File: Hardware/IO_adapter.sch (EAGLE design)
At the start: 20 parts, among them Y1 32Khz

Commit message: rough layout top board
I have not double checked the board to board interconect yet.
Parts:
- added PRG, RST: 6X3.5_TACT, tactile_switch:6X3.5_TACT
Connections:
- net ADCCS1: now also PRG.1
- net GND: now also PRG.2, RST.2
- net RST: now also RST.1
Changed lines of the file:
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@@
 <part name="LED1" library="adafruit" deviceset="LED" device="CHIPLED_0805"/>
 <part name="LED2" library="adafruit" deviceset="LED" device="CHIPLED_0805"/>
+<part name="PRG" library="tactile_switch" deviceset="6X3.5_TACT" device=""/>
+<part name="RST" library="tactile_switch" deviceset="6X3.5_TACT" device=""/>
+<part name="GND1" library="supply1" deviceset="GND" device=""/>
 </parts>
 <sheets>
@@
 <instance part="LED1" gate="G$1" x="86.36" y="91.44" rot="R90"/>
 <instance part="LED2" gate="G$1" x="88.9" y="86.36" rot="R270"/>
+<instance part="PRG" gate="G$1" x="223.52" y="-53.34"/>
+<instance part="RST" gate="G$1" x="223.52" y="-66.04"/>
+<instance part="GND1" gate="1" x="243.84" y="-78.74"/>
 </instances>
 <busses>
@@
 <pinref part="C7" gate="G$1" pin="2"/>
 <wire x1="261.62" y1="63.5" x2="259.08" y2="63.5" width="0.1524" layer="91"/>
+</segment>
+<segment>
+<pinref part="PRG" gate="G$1" pin="2"/>
+<wire x1="231.14" y1="-53.34" x2="243.84" y2="-53.34" width="0.1524" layer="91"/>
+<wire x1="243.84" y1="-53.34" x2="243.84" y2="-66.04" width="0.1524" layer="91"/>
+<pinref part="RST" gate="G$1" pin="2"/>
+<wire x1="243.84" y1="-66.04" x2="243.84" y2="-76.2" width="0.1524" layer="91"/>
+<wire x1="231.14" y1="-66.04" x2="243.84" y2="-66.04" width="0.1524" layer="91"/>
+<junction x="243.84" y="-66.04"/>
+<pinref part="GND1" gate="1" pin="GND"/>
 </segment>
 </net>
@@
 <label x="261.62" y="5.08" size="1.778" layer="91" font="vector" xref="yes"/>
 </segment>
+<segment>
+<pinref part="PRG" gate="G$1" pin="1"/>
+<wire x1="218.44" y1="-53.34" x2="210.82" y2="-53.34" width="0.1524" layer="91"/>
+<label x="210.82" y="-53.34" size="1.778" layer="95" rot="R180" xref="yes"/>
+</segment>
 </net>
 <net name="CSSD" class="0">
@@
 <label x="261.62" y="-17.78" size="1.778" layer="91" font="vector" xref="yes"/>
 </segment>
-</net>
+<segment>
+<pinref part="RST" gate="G$1" pin="1"/>
+<wire x1="218.44" y1="-66.04" x2="210.82" y2="-66.04" width="0.1524" layer="91"/>
+<label x="210.82" y="-66.04" size="1.778" layer="95" rot="R180" xref="yes"/>
+</segment>
+</net>

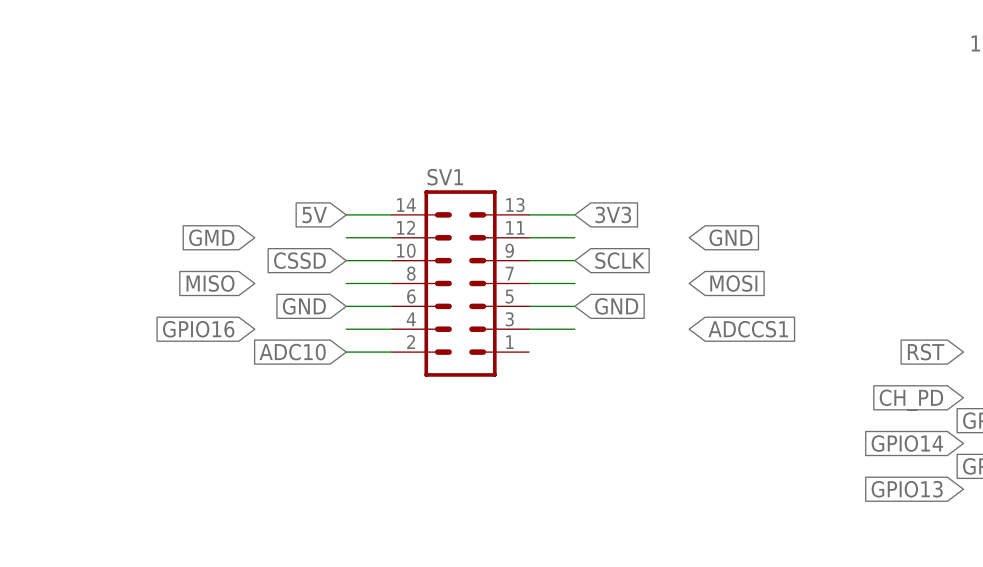
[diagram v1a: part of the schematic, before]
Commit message: completed routing for both boards
routed out both the base and IO board. Should be ready for verification
There will be errors.
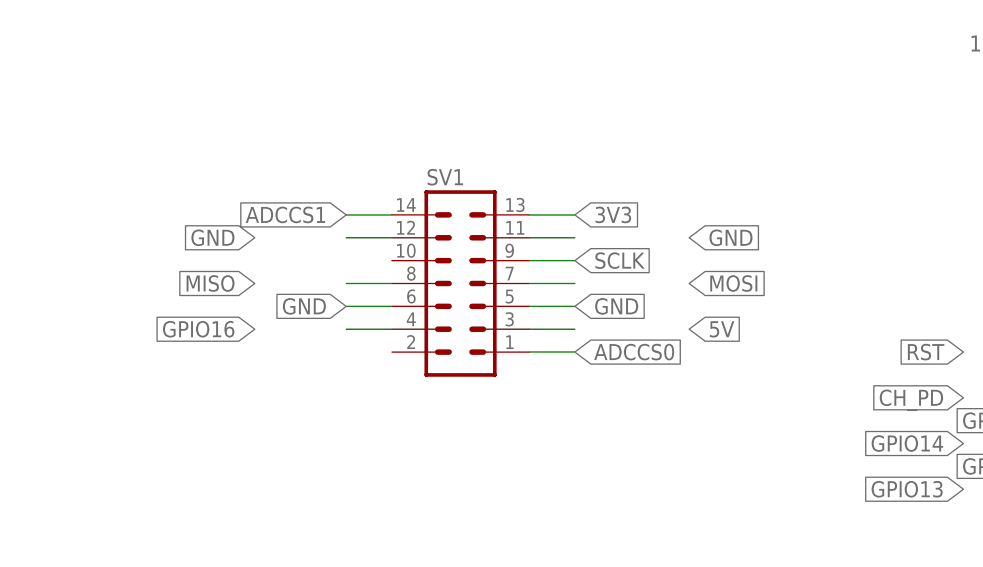
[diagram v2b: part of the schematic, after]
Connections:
- removed net ADC10: SV1.2
- removed net GMD: SV1.12
- net 5V: now also SV1.3; no longer SV1.14
- net ADCCS0: now also SV1.1
- net ADCCS1: now also SV1.14; no longer SV1.3
- net CSSD: no longer SV1.10
- net GND: now also SV1.12
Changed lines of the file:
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@@
 <pinref part="GND1" gate="1" pin="GND"/>
+</segment>
+<segment>
+<pinref part="SV1" gate="G$1" pin="12"/>
+<wire x1="71.12" y1="17.78" x2="66.04" y2="17.78" width="0.1524" layer="91"/>
+<label x="55.88" y="17.78" size="1.778" layer="91" font="vector" rot="R180" xref="yes"/>
 </segment>
 </net>
@@
 </segment>
 <segment>
-<pinref part="SV1" gate="G$1" pin="3"/>
-<wire x1="86.36" y1="7.62" x2="91.44" y2="7.62" width="0.1524" layer="91"/>
-<label x="104.14" y="7.62" size="1.778" layer="91" font="vector" xref="yes"/>
-</segment>
-<segment>
 <pinref part="U1" gate="G$1" pin="GPIO0"/>
 <wire x1="182.88" y1="-5.08" x2="187.96" y2="-5.08" width="0.1524" layer="91"/>
@@
 <wire x1="218.44" y1="-53.34" x2="210.82" y2="-53.34" width="0.1524" layer="91"/>
 <label x="210.82" y="-53.34" size="1.778" layer="95" rot="R180" xref="yes"/>
+</segment>
+<segment>
+<pinref part="SV1" gate="G$1" pin="14"/>
+<wire x1="71.12" y1="20.32" x2="66.04" y2="20.32" width="0.1524" layer="91"/>
+<label x="66.04" y="20.32" size="1.778" layer="91" rot="R180" xref="yes"/>
 </segment>
 </net>
@@
 </segment>
 <segment>
-<pinref part="SV1" gate="G$1" pin="10"/>
-<wire x1="71.12" y1="15.24" x2="66.04" y2="15.24" width="0.1524" layer="91"/>
-<label x="66.04" y="15.24" size="1.778" layer="91" font="vector" rot="R180" xref="yes"/>
-</segment>
-<segment>
 <pinref part="U1" gate="G$1" pin="CS0"/>
 <wire x1="160.02" y1="-30.48" x2="160.02" y2="-45.72" width="0.1524" layer="91"/>
 <label x="160.02" y="-45.72" size="1.778" layer="91" rot="R270" xref="yes"/>
-</segment>
-</net>
-<net name="ADC10" class="0">
-<segment>
-<pinref part="SV1" gate="G$1" pin="2"/>
-<wire x1="71.12" y1="5.08" x2="66.04" y2="5.08" width="0.1524" layer="91"/>
-<label x="66.04" y="5.08" size="1.778" layer="91" font="vector" rot="R180" xref="yes"/>
 </segment>
 </net>
@@
 </segment>
 <segment>
-<pinref part="SV1" gate="G$1" pin="14"/>
-<wire x1="66.04" y1="20.32" x2="71.12" y2="20.32" width="0.1524" layer="91"/>
-<label x="66.04" y="20.32" size="1.778" layer="91" font="vector" rot="R180" xref="yes"/>
+<pinref part="SV1" gate="G$1" pin="3"/>
+<wire x1="86.36" y1="7.62" x2="91.44" y2="7.62" width="0.1524" layer="91"/>
+<label x="104.14" y="7.62" size="1.778" layer="95" xref="yes"/>
 </segment>
 </net>
@@
 </segment>
 </net>
-<net name="GMD" class="0">
-<segment>
-<pinref part="SV1" gate="G$1" pin="12"/>
-<wire x1="71.12" y1="17.78" x2="66.04" y2="17.78" width="0.1524" layer="91"/>
-<label x="55.88" y="17.78" size="1.778" layer="91" font="vector" rot="R180" xref="yes"/>
-</segment>
-</net>
 <net name="ADCCS0" class="0">
 <segment>
@@
 <label x="261.62" y="-2.54" size="1.778" layer="91" font="vector" xref="yes"/>
 </segment>
-</net>
+<segment>
+<pinref part="SV1" gate="G$1" pin="1"/>
+<wire x1="86.36" y1="5.08" x2="91.44" y2="5.08" width="0.1524" layer="91"/>
+<label x="91.44" y="5.08" size="1.778" layer="95" xref="yes"/>
+</segment>
+</net>

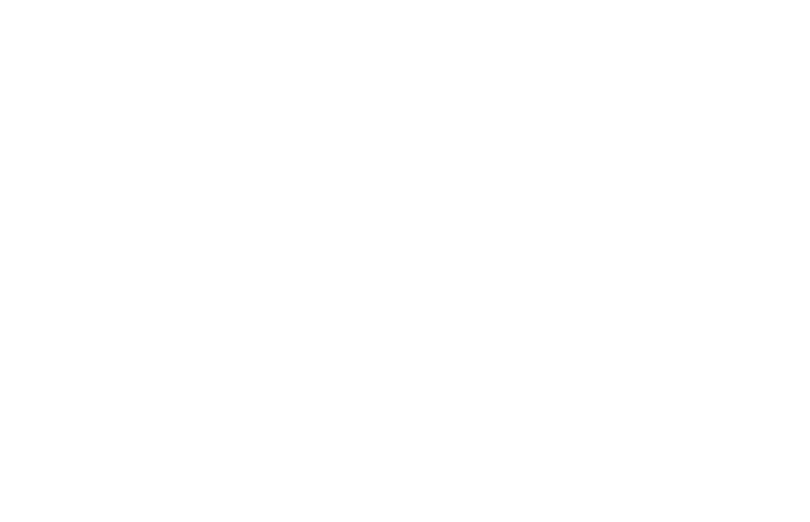
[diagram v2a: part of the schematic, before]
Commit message: added the programming header
I had forgotten the programming header. It's right there now.
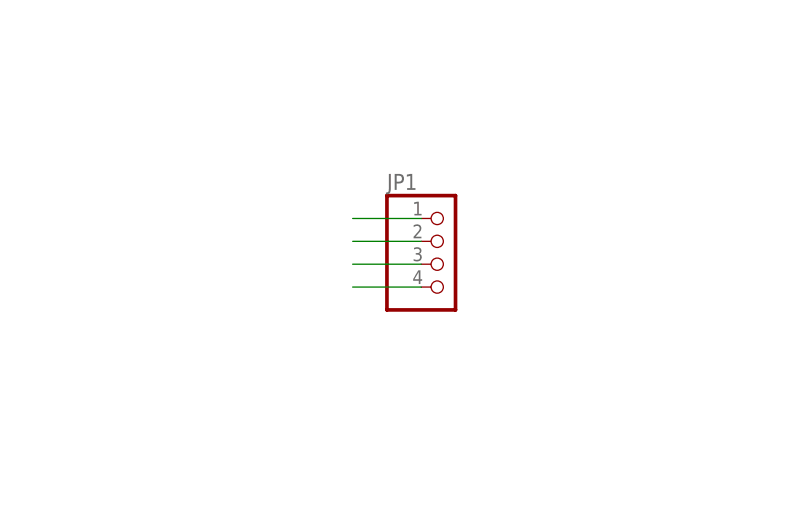
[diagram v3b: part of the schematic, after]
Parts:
- added JP1: (no value), pinhead:PINHD-1X4
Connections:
- net 3V3: now also JP1.1
- net GND: now also JP1.4
- net RXD: now also JP1.2
- net TXD: now also JP1.3
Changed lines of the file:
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@@
 <part name="RST" library="tactile_switch" deviceset="6X3.5_TACT" device=""/>
 <part name="GND1" library="supply1" deviceset="GND" device=""/>
+<part name="JP1" library="pinhead" deviceset="PINHD-1X4" device=""/>
 </parts>
 <sheets>
@@
 <instance part="RST" gate="G$1" x="223.52" y="-66.04"/>
 <instance part="GND1" gate="1" x="243.84" y="-78.74"/>
+<instance part="JP1" gate="A" x="170.18" y="86.36"/>
 </instances>
 <busses>
@@
 <wire x1="71.12" y1="17.78" x2="66.04" y2="17.78" width="0.1524" layer="91"/>
 <label x="55.88" y="17.78" size="1.778" layer="91" font="vector" rot="R180" xref="yes"/>
+</segment>
+<segment>
+<pinref part="JP1" gate="A" pin="4"/>
+<wire x1="167.64" y1="83.82" x2="160.02" y2="83.82" width="0.1524" layer="91"/>
 </segment>
 </net>
@@
 <junction x="271.78" y="53.34"/>
 </segment>
+<segment>
+<pinref part="JP1" gate="A" pin="1"/>
+<wire x1="167.64" y1="91.44" x2="160.02" y2="91.44" width="0.1524" layer="91"/>
+</segment>
 </net>
 <net name="ADCCS1" class="0">
@@
 <label x="200.66" y="5.08" size="1.778" layer="91" xref="yes"/>
 </segment>
+<segment>
+<pinref part="JP1" gate="A" pin="3"/>
+<wire x1="167.64" y1="86.36" x2="160.02" y2="86.36" width="0.1524" layer="91"/>
+</segment>
 </net>
 <net name="RXD" class="0">
@@
 <label x="187.96" y="2.54" size="1.778" layer="91" xref="yes"/>
 </segment>
-</net>
+<segment>
+<pinref part="JP1" gate="A" pin="2"/>
+<wire x1="167.64" y1="88.9" x2="160.02" y2="88.9" width="0.1524" layer="91"/>
+</segment>
+</net>

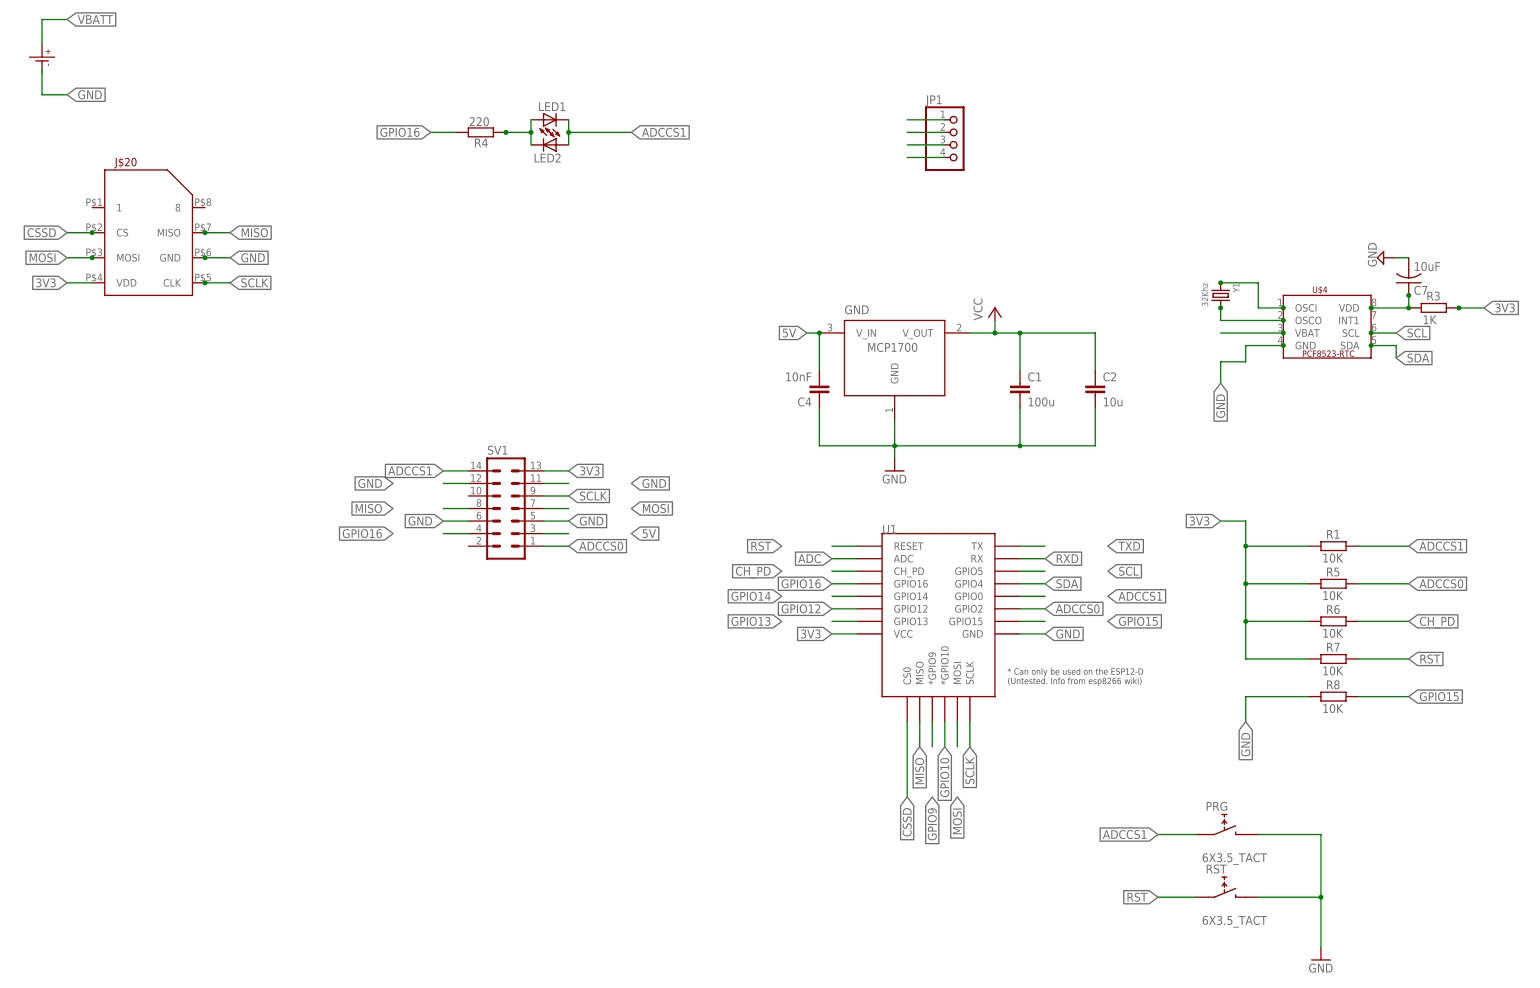
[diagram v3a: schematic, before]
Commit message: beginning to add a 2.2" TFT display
not quite sure about the mechanical layout yet.
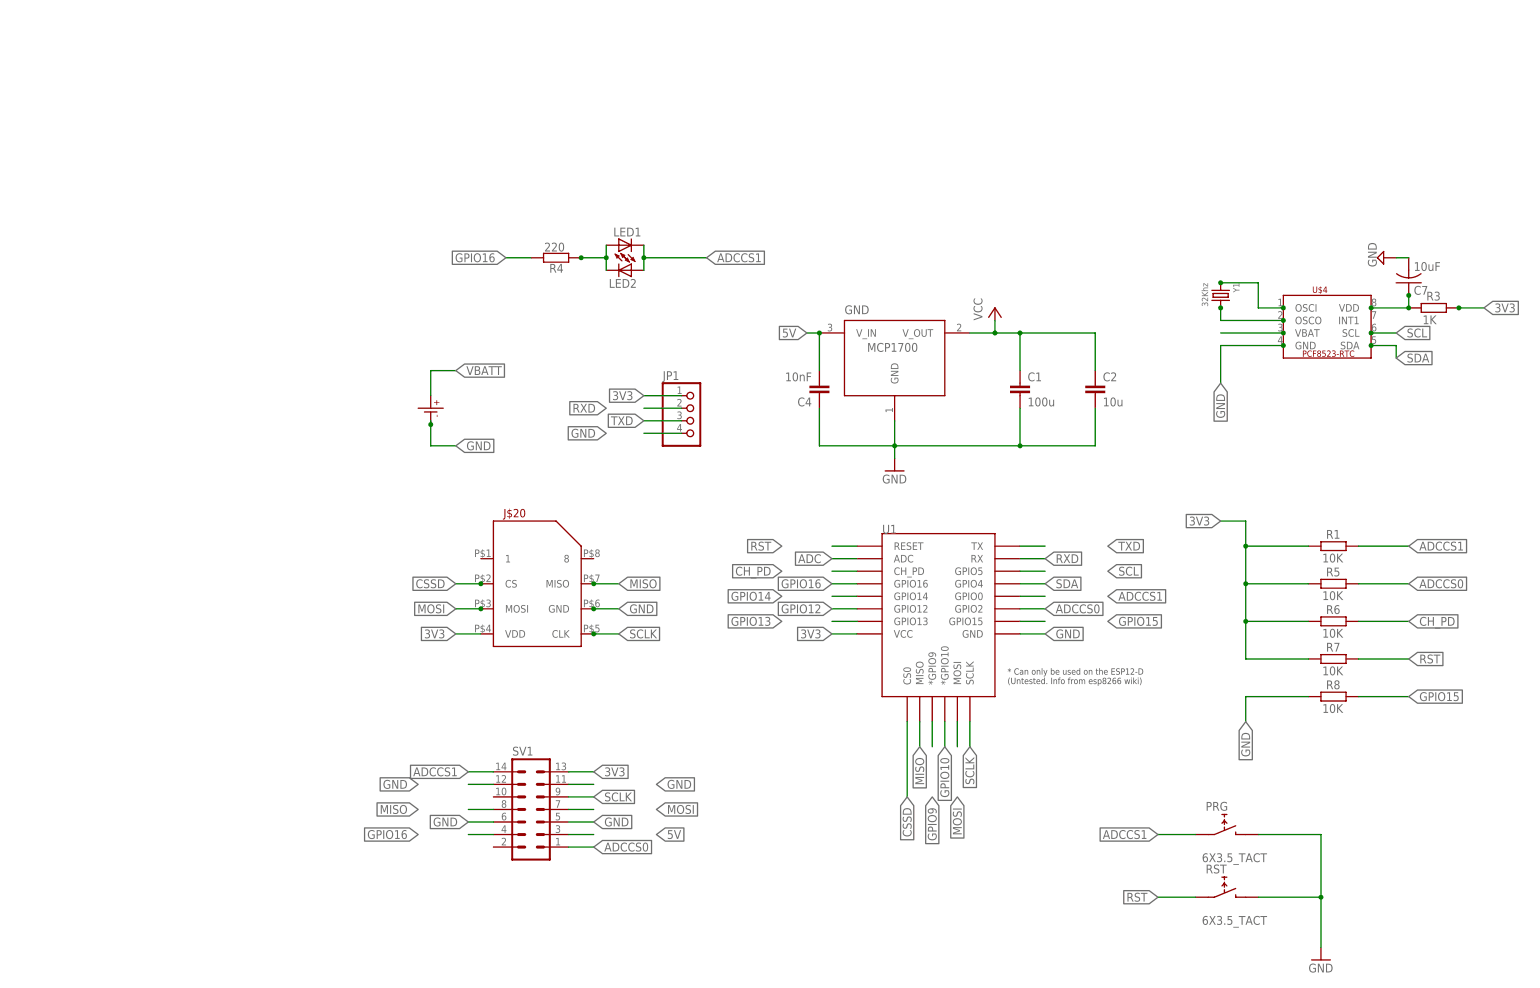
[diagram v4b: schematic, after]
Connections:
- net GND: now also U$1.P$-
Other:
- moved on the sheet: J$20, JP1, LED1, LED2, R4, SV1

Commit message: Revert "beginning to add a 2.2" TFT display"
This reverts commit 5a3055f75d7c66bfc0e3a1cc9d4d5180e17e1807.
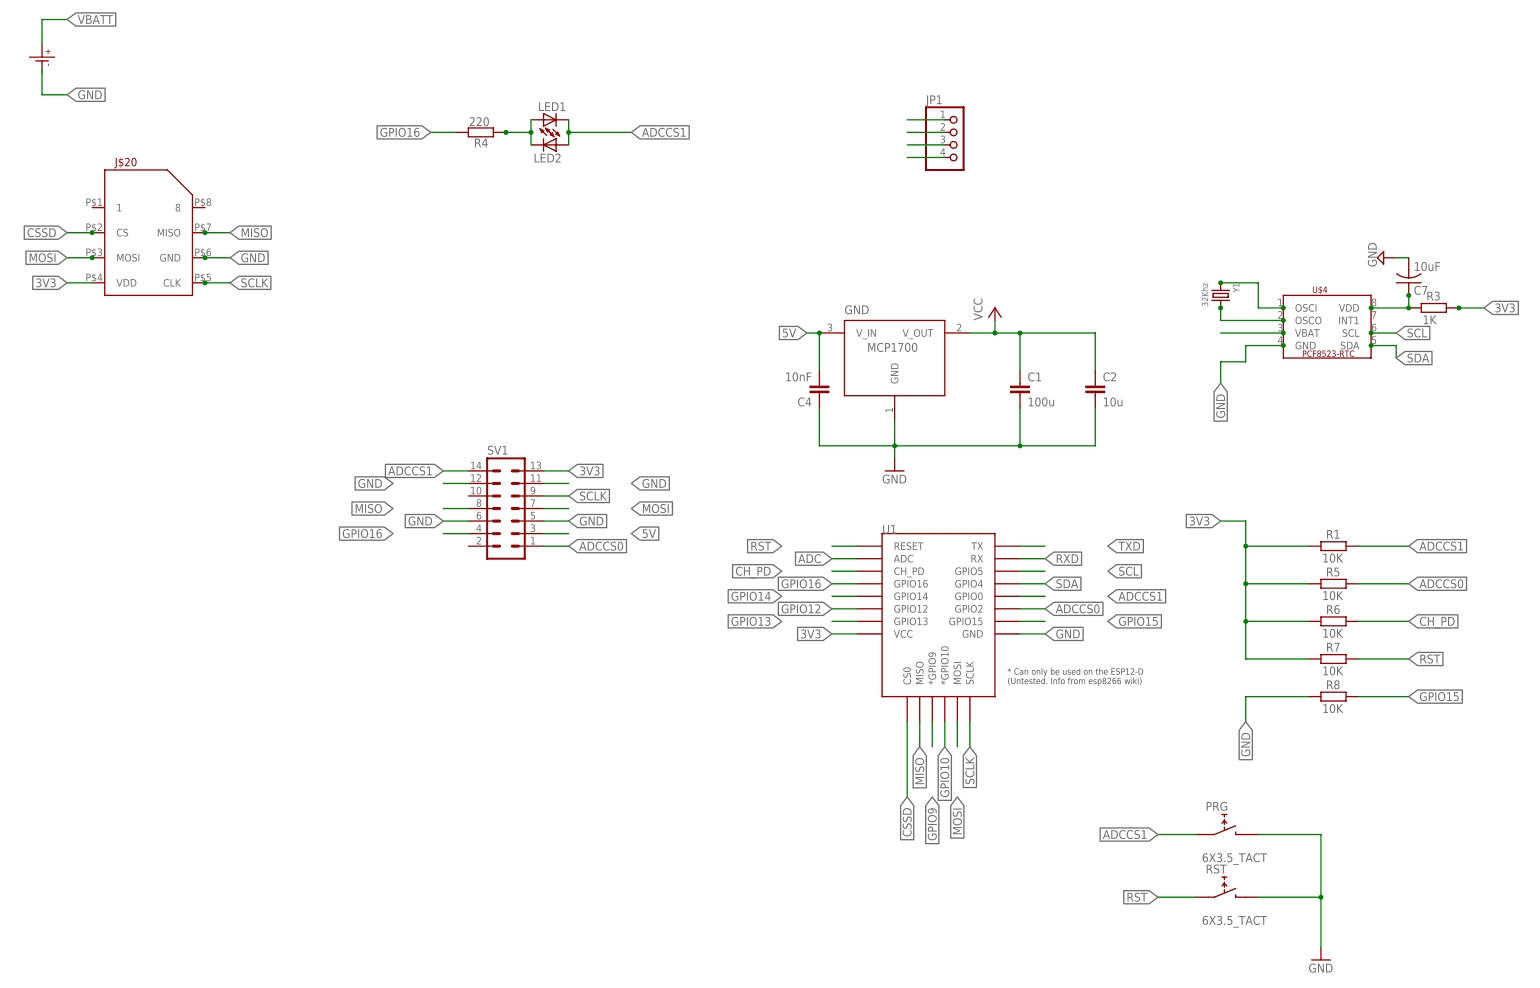
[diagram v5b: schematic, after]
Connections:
- net GND: no longer U$1.P$-
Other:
- moved on the sheet: J$20, JP1, LED1, LED2, R4, SV1
